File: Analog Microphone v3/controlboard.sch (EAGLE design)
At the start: 30 parts, among them J2 USB_A_SMT_FEMALE, Q1 12MHz

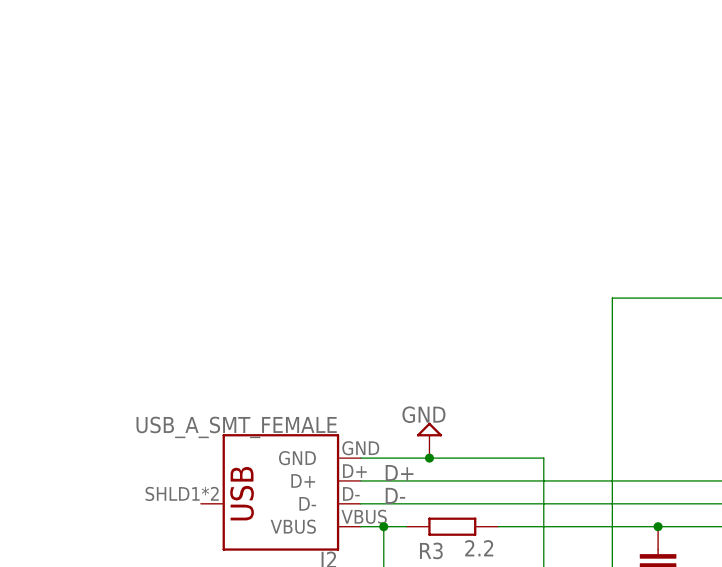
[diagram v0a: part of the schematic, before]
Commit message: Added bottom ground plane + usb test headers
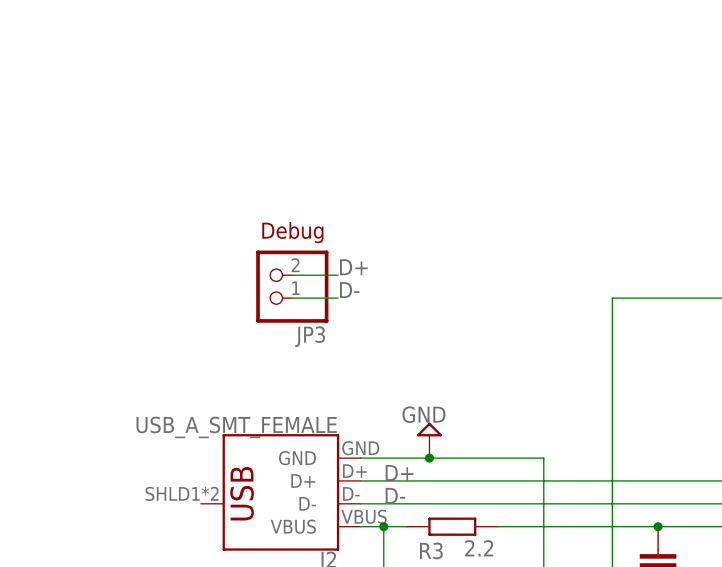
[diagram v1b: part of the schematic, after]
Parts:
- added JP3: (no value), pinhead:PINHD-1X2
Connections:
- net D+: now also JP3.2
- net D-: now also JP3.1
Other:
- note added: "Debug"
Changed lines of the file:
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@@
 <part name="SUPPLY2" library="supply2" library_urn="urn:adsk.eagle:library:372" deviceset="GND" device=""/>
 <part name="SUPPLY6" library="supply2" library_urn="urn:adsk.eagle:library:372" deviceset="GND" device=""/>
+<part name="JP3" library="pinhead" library_urn="urn:adsk.eagle:library:325" deviceset="PINHD-1X2" device="" package3d_urn="urn:adsk.eagle:package:22435/2"/>
 </parts>
 <sheets>
@@
 <text x="-27.94" y="91.44" size="3.81" layer="94">Microphone Connectors</text>
 <text x="40.64" y="-40.64" size="1.778" layer="94">Speaker out</text>
+<text x="-94.996" y="54.864" size="1.778" layer="94">Debug</text>
 </plain>
 <instances>
@@
 <instance part="SUPPLY6" gate="GND" x="-88.9" y="-58.42" smashed="yes">
 <attribute name="VALUE" x="-90.805" y="-61.595" size="1.778" layer="96"/>
+</instance>
+<instance part="JP3" gate="G$1" x="-93.98" y="50.8" smashed="yes" rot="R180">
+<attribute name="NAME" x="-87.63" y="45.085" size="1.778" layer="95" rot="R180"/>
+<attribute name="VALUE" x="-87.63" y="55.88" size="1.778" layer="96" rot="R180"/>
 </instance>
 </instances>
@@
 <wire x1="-38.1" y1="27.94" x2="-83.82" y2="27.94" width="0.1524" layer="91"/>
 </segment>
+<segment>
+<pinref part="JP3" gate="G$1" pin="2"/>
+<wire x1="-91.44" y1="50.8" x2="-86.36" y2="50.8" width="0.1524" layer="91"/>
+<label x="-86.36" y="50.8" size="1.778" layer="95"/>
+</segment>
 </net>
 <net name="D-" class="0">
@@
 <wire x1="-83.82" y1="25.4" x2="-33.02" y2="25.4" width="0.1524" layer="91"/>
 </segment>
-</net>
+<segment>
+<pinref part="JP3" gate="G$1" pin="1"/>
+<wire x1="-91.44" y1="48.26" x2="-86.36" y2="48.26" width="0.1524" layer="91"/>
+<label x="-86.36" y="48.26" size="1.778" layer="95"/>
+</segment>
+</net>
